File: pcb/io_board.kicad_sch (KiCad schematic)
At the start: 40 parts

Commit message: Further schematic capture
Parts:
- J?: value Barrel_Jack -> 9-15V DC
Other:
- note added: "ADAT Terminals"
- note added: "IDC Connector"
- note added: "Power Supply: 9-15V -SMPS-> 5V -LDO-> 3V3"
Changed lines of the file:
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@@
 		)
 	)
+	(text "IDC Connector"
+		(exclude_from_sim no)
+		(at 54.356 77.724 0)
+		(effects
+			(font
+				(size 2.54 2.54)
+				(thickness 0.3175)
+			)
+		)
+	)
+	(text "Power Supply: 9-15V -SMPS-> 5V -LDO-> 3V3"
+		(exclude_from_sim no)
+		(at 147.828 19.558 0)
+		(effects
+			(font
+				(size 2.54 2.54)
+				(thickness 0.3175)
+			)
+		)
+	)
+	(text "ADAT Terminals"
+		(exclude_from_sim no)
+		(at 186.69 80.518 0)
+		(effects
+			(font
+				(size 2.54 2.54)
+				(thickness 0.3175)
+			)
+		)
+	)
 	(junction
 		(at 186.69 35.56)
@@
 			)
 		)
-		(property "Value" "Barrel_Jack"
+		(property "Value" "9-15V DC"
 			(at 39.37 31.75 0)
 			(effects

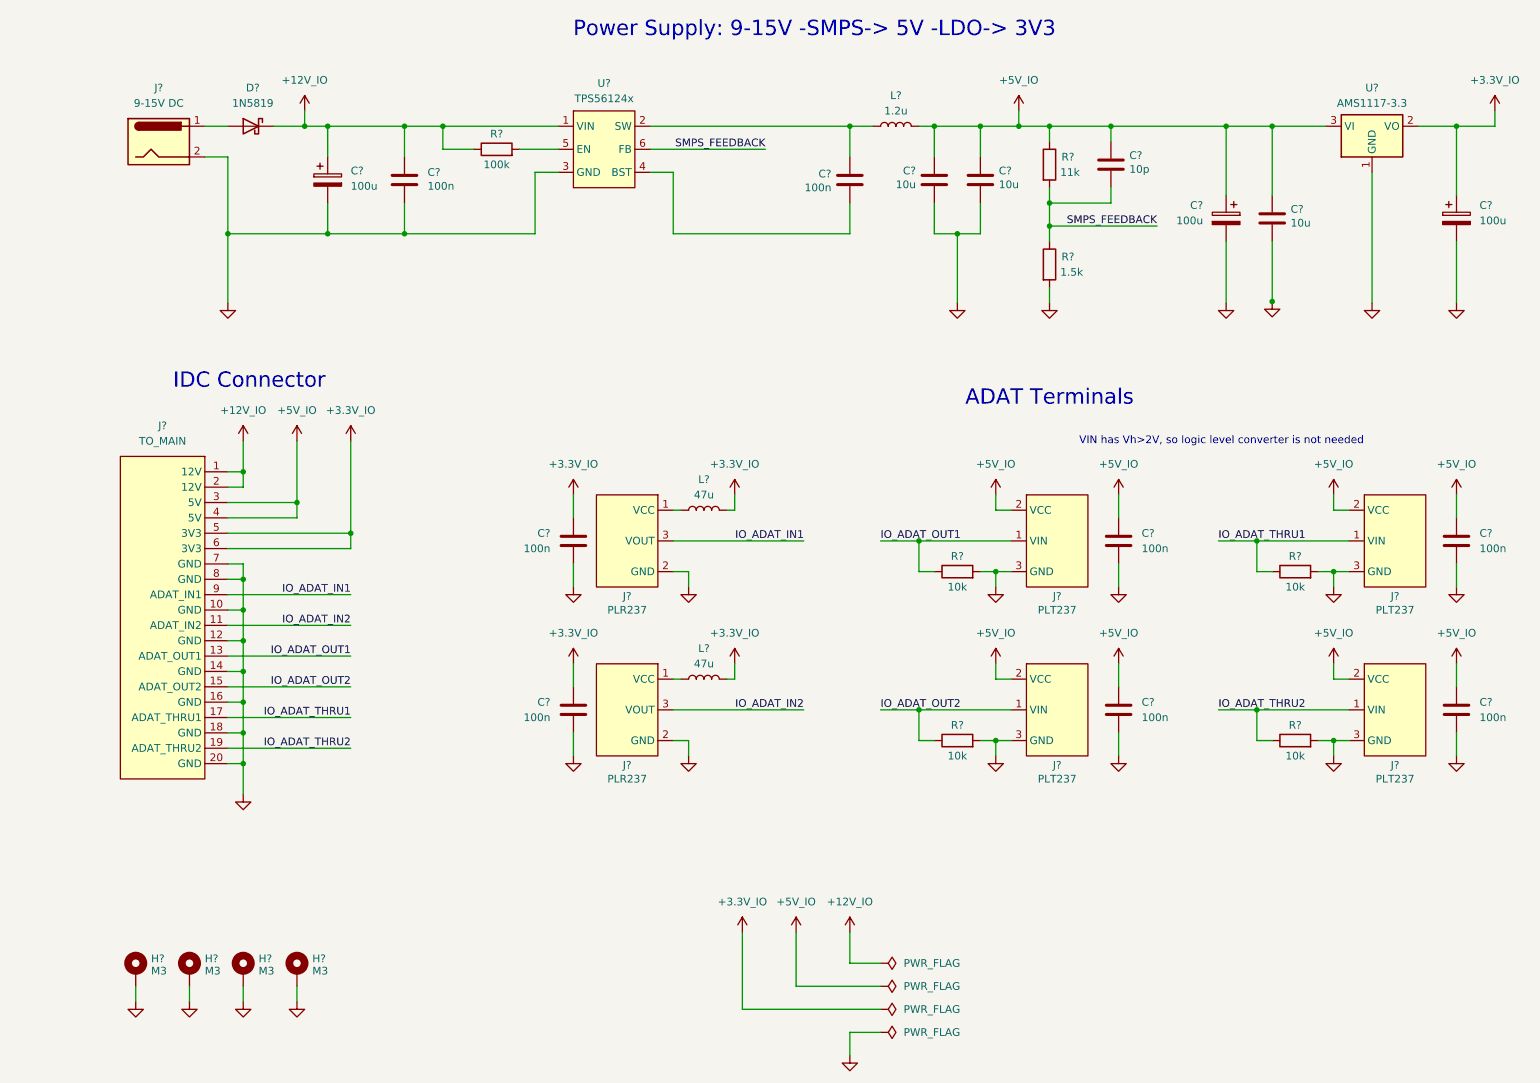
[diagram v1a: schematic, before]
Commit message: Assign most of the footprints to schematic components
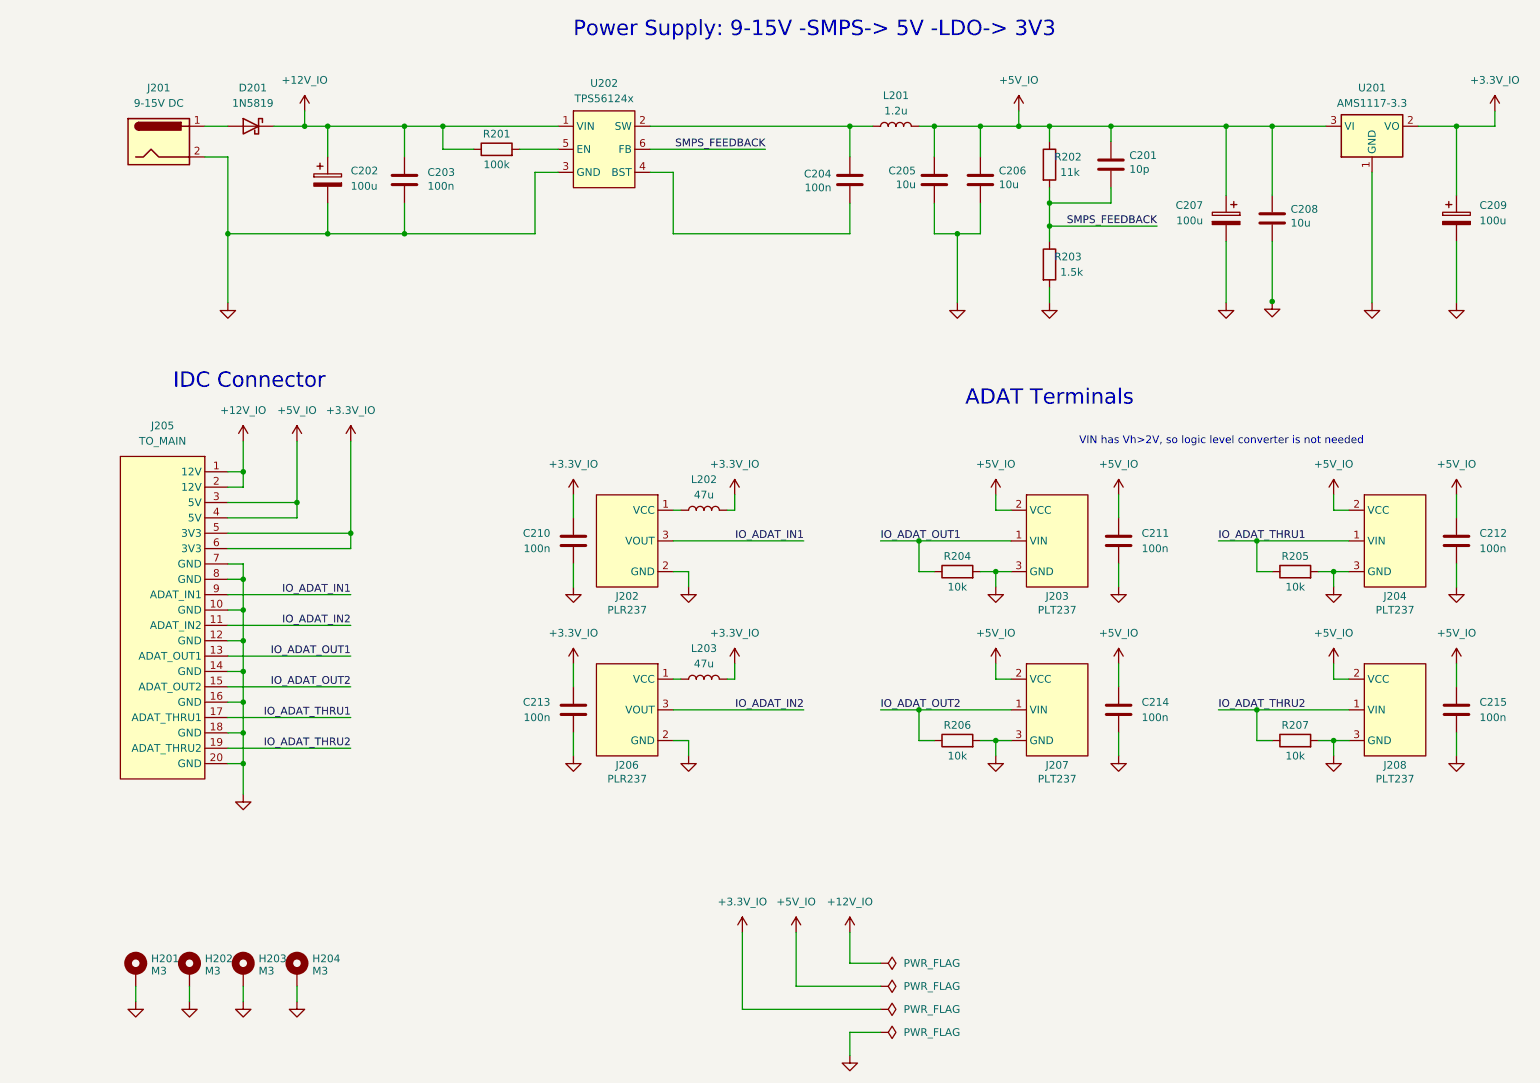
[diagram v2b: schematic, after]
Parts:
- C201, C203, C204, C205, C206, C208, C210, C211, C212, C213, C214, C215: renamed from C?; footprint (none) -> Capacitor_SMD:C_0805_2012Metric_Pad1.18x1.45mm_HandSolder
- C202, C207, C209: renamed from C?; footprint (none) -> Capacitor_SMD:C_Elec_6.3x5.4
- J205: renamed from J?; footprint (none) -> Connector_IDC:IDC-Header_2x10_P2.54mm_Vertical
- R201, R202, R203, R204, R205, R206, R207: renamed from R?; footprint (none) -> Resistor_SMD:R_0805_2012Metric_Pad1.20x1.40mm_HandSolder
- gave numbers to parts that had none: 17

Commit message: Finish assigning footprints to project
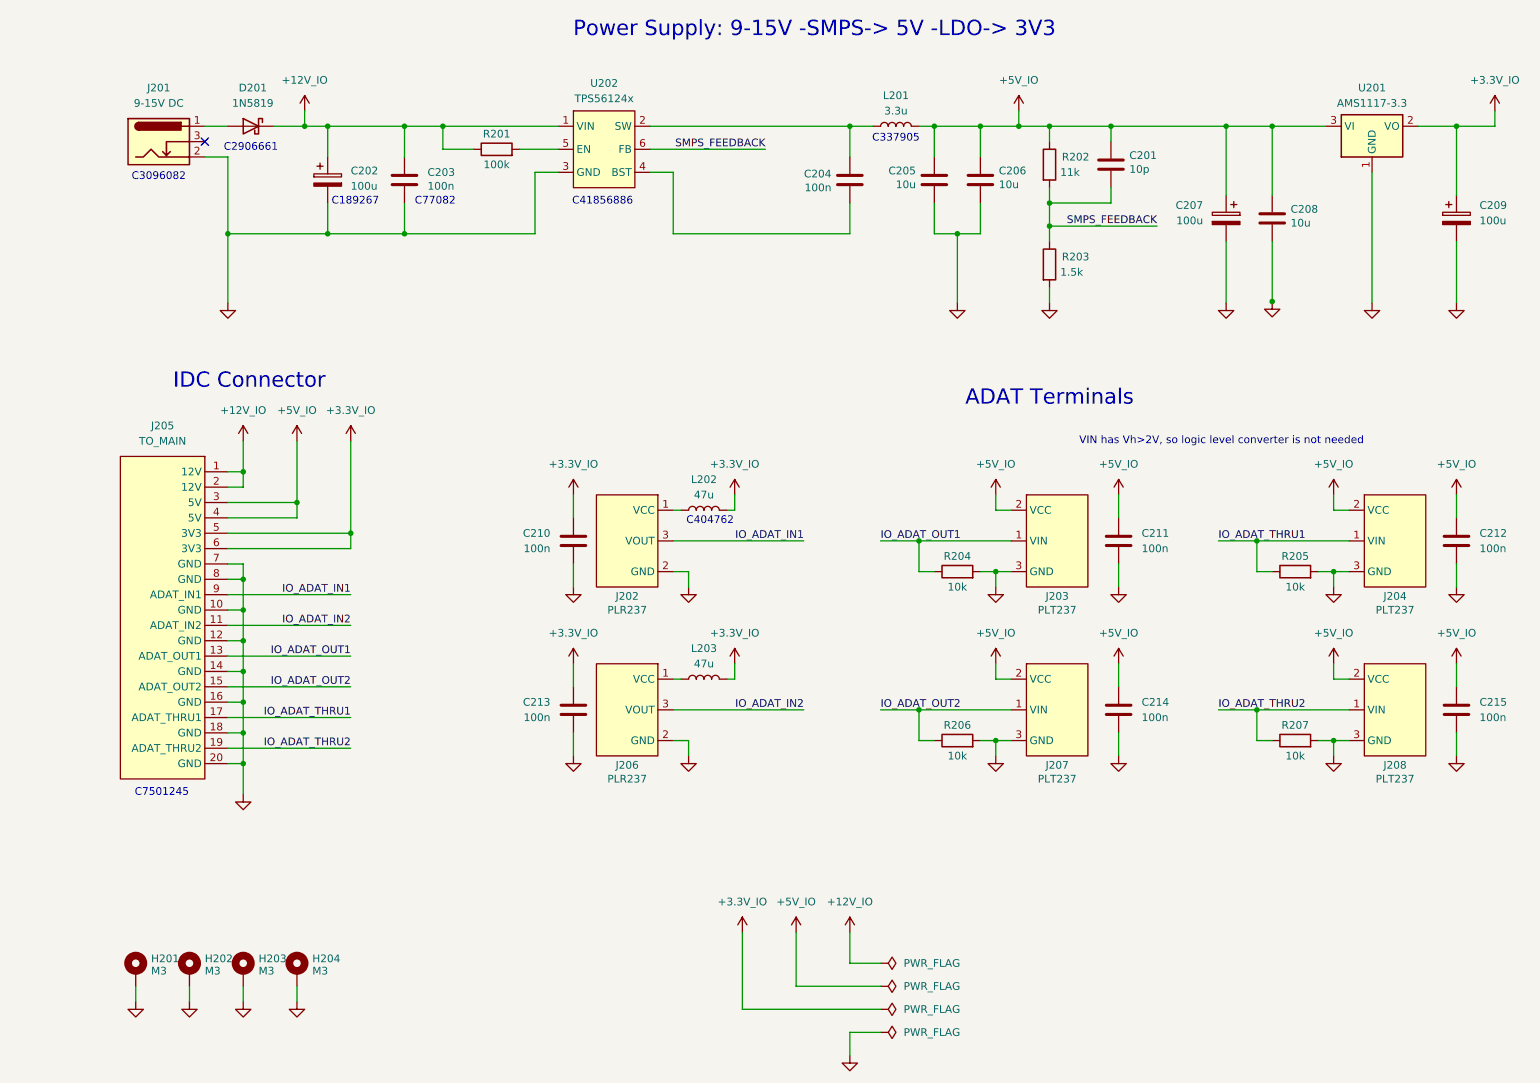
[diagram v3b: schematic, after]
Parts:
- removed J201: 9-15V DC, symbol Connector:Barrel_Jack
- added J201: 9-15V DC, adatv2:CUI PJ-002A, symbol Connector:Barrel_Jack_Switch
- L201: value 1.2u -> 3.3u; footprint (none) -> Inductor_SMD:L_1210_3225Metric_Pad1.42x2.65mm_HandSolder
- L202, L203: footprint (none) -> Inductor_SMD:L_0805_2012Metric_Pad1.15x1.40mm_HandSolder
- U202: footprint (none) -> Package_TO_SOT_SMD:SOT-563
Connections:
- net GND_IO: now also J201.2
- net at D201.2 (A): now also J201.1
- no-connect marks 0 -> 1
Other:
- note added: "C189267"
- note added: "C2906661"
- note added: "C3096082"
- note added: "C337905"
- note added: "C404762"
- note added: "C41856886"
- note added: "C7501245"
- note added: "C77082"
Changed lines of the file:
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@@
 		(comment 1 "Drawn by Łukasz Świszcz")
 	)
+	(text "C41856886"
+		(exclude_from_sim no)
+		(at 112.776 48.006 0)
+		(effects
+			(font
+				(size 1.27 1.27)
+			)
+		)
+	)
+	(text "C189267"
+		(exclude_from_sim no)
+		(at 71.882 48.006 0)
+		(effects
+			(font
+				(size 1.27 1.27)
+			)
+		)
+	)
+	(text "C404762"
+		(exclude_from_sim no)
+		(at 130.556 100.838 0)
+		(effects
+			(font
+				(size 1.27 1.27)
+			)
+		)
+	)
+	(text "C3096082"
+		(exclude_from_sim no)
+		(at 39.37 43.942 0)
+		(effects
+			(font
+				(size 1.27 1.27)
+			)
+		)
+	)
+	(text "C337905"
+		(exclude_from_sim no)
+		(at 161.29 37.592 0)
+		(effects
+			(font
+				(size 1.27 1.27)
+			)
+		)
+	)
+	(text "C2906661"
+		(exclude_from_sim no)
+		(at 54.61 39.116 0)
+		(effects
+			(font
+				(size 1.27 1.27)
+			)
+		)
+	)
+	(text "C7501245"
+		(exclude_from_sim no)
+		(at 39.878 145.796 0)
+		(effects
+			(font
+				(size 1.27 1.27)
+			)
+		)
+	)
 	(text "VIN has Vh>2V, so logic level converter is not needed"
 		(exclude_from_sim no)
@@
 		)
 	)
+	(text "C77082"
+		(exclude_from_sim no)
+		(at 85.09 48.006 0)
+		(effects
+			(font
+				(size 1.27 1.27)
+			)
+		)
+	)
 	(text "IDC Connector"
 		(exclude_from_sim no)
@@
 		(color 0 0 0 0)
 	)
+	(no_connect
+		(at 46.99 38.1)
+	)
 	(wire
 		(pts
@@
 	)
 	(symbol
+		(lib_id "Connector:Barrel_Jack_Switch")
+		(at 39.37 38.1 0)
+		(unit 1)
+		(exclude_from_sim no)
+		(in_bom yes)
+		(on_board yes)
+		(dnp no)
+		(fields_autoplaced yes)
+		(property "Reference" "J201"
+			(at 39.37 29.21 0)
+			(effects
+				(font
+					(size 1.27 1.27)
+				)
+			)
+		)
+		(property "Value" "9-15V DC"
+			(at 39.37 31.75 0)
+			(effects
+				(font
+					(size 1.27 1.27)
+				)
+			)
+		)
+		(property "Footprint" "adatv2:CUI PJ-002A"
+			(at 40.64 39.116 0)
+			(effects
+				(font
+					(size 1.27 1.27)
+				)
+				(hide yes)
+			)
+		)
+		(property "Datasheet" "~"
+			(at 40.64 39.116 0)
+			(effects
+				(font
+					(size 1.27 1.27)
+				)
+				(hide yes)
+			)
+		)
+		(property "Description" "DC Barrel Jack with an internal switch"
+			(at 39.37 38.1 0)
+			(effects
+				(font
+					(size 1.27 1.27)
+				)
+				(hide yes)
+			)
+		)
+		(pin "3"
+		)
+		(pin "1"
+		)
+		(pin "2"
+		)
+		(instances
+			(project ""
+				(path "/81929cdc-f9fd-4c47-8b7e-bc8597104756/2798f55d-c401-4d3b-b8be-ffe1fd6e245a"
+					(reference "J201")
+					(unit 1)
+				)
+			)
+		)
+	)
+	(symbol
 		(lib_id "power:GND")
 		(at 107.95 139.7 0)
@@
 			)
 		)
-		(property "Footprint" ""
+		(property "Footprint" "Inductor_SMD:L_0805_2012Metric_Pad1.15x1.40mm_HandSolder"
 			(at 129.54 127 0)
 			(effects
@@
 		(dnp no)
 		(property "Reference" "R202"
-			(at 189.738 40.64 0)
+			(at 191.008 40.64 0)
 			(effects
 				(font
@@
 		(dnp no)
 		(property "Reference" "R203"
-			(at 189.738 57.15 0)
+			(at 191.008 57.15 0)
 			(effects
 				(font
@@
 			)
 		)
-		(property "Footprint" ""
+		(property "Footprint" "Inductor_SMD:L_0805_2012Metric_Pad1.15x1.40mm_HandSolder"
 			(at 129.54 99.06 0)
 			(effects
@@
 	)
 	(symbol
-		(lib_id "Connector:Barrel_Jack")
-		(at 39.37 38.1 0)
-		(unit 1)
-		(exclude_from_sim no)
-		(in_bom yes)
-		(on_board yes)
-		(dnp no)
-		(fields_autoplaced yes)
-		(property "Reference" "J201"
-			(at 39.37 29.21 0)
-			(effects
-				(font
-					(size 1.27 1.27)
-				)
-			)
-		)
-		(property "Value" "9-15V DC"
-			(at 39.37 31.75 0)
-			(effects
-				(font
-					(size 1.27 1.27)
-				)
-			)
-		)
-		(property "Footprint" ""
-			(at 40.64 39.116 0)
-			(effects
-				(font
-					(size 1.27 1.27)
-				)
-				(hide yes)
-			)
-		)
-		(property "Datasheet" "~"
-			(at 40.64 39.116 0)
-			(effects
-				(font
-					(size 1.27 1.27)
-				)
-				(hide yes)
-			)
-		)
-		(property "Description" "DC Barrel Jack"
-			(at 39.37 38.1 0)
-			(effects
-				(font
-					(size 1.27 1.27)
-				)
-				(hide yes)
-			)
-		)
-		(pin "1"
-		)
-		(pin "2"
-		)
-		(instances
-			(project "adatv2"
-				(path "/81929cdc-f9fd-4c47-8b7e-bc8597104756/2798f55d-c401-4d3b-b8be-ffe1fd6e245a"
-					(reference "J201")
-					(unit 1)
-				)
-			)
-		)
-	)
-	(symbol
 		(lib_id "power:PWR_FLAG")
 		(at 158.75 181.61 270)
@@
 			)
 		)
-		(property "Value" "1.2u"
+		(property "Value" "3.3u"
 			(at 161.29 33.02 90)
 			(effects
@@
 			)
 		)
-		(property "Footprint" ""
+		(property "Footprint" "Inductor_SMD:L_1210_3225Metric_Pad1.42x2.65mm_HandSolder"
 			(at 161.29 35.56 0)
 			(effects
@@
 			)
 		)
-		(property "Footprint" ""
+		(property "Footprint" "Package_TO_SOT_SMD:SOT-563"
 			(at 113.03 39.37 0)
 			(effects

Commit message: Finish drawing IO/Supply board
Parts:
- added TP201, TP202, TP203: ${NET_NAME(1)}, TestPoint:TestPoint_Pad_D2.5mm, symbol Connector:TestPoint
- C205, C206, C208: footprint Capacitor_SMD:C_0805_2012Metric_Pad1.18x1.45mm_HandSolder -> Capacitor_SMD:C_1206_3216Metric_Pad1.33x1.80mm_HandSolder
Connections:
- net GND is gone; now on net GND_IO: H201.1, H202.1, H203.1, H204.1
- net +12V_IO: now also TP201.1
- net +3.3V_IO: now also L202.1, L203.1, TP203.1; no longer C210.1, C213.1, L202.2, L203.2
- net +5V_IO: now also TP202.1
- net POWER_IN: now reaches D201.2 (A), J201.1
- net at J206.1 (VCC): now also C213.1, L203.2; no longer L203.1
- net at J202.1 (VCC): now also C210.1, L202.2; no longer L202.1
- net SMPS_POWER_OUT: now reaches C204.1, L201.1, U202.2 (SW)
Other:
- moved on the sheet: J201, L202, L203

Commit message: Add buffers for ADAT transfer
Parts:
- added C216: 100n, Capacitor_SMD:C_0805_2012Metric_Pad1.18x1.45mm_HandSolder, symbol Device:C
- added U203: 74LVC2G17, Package_TO_SOT_SMD:SOT-23-6_Handsoldering, symbol 74xGxx:74LVC2G17
- R204, R205, R206, R207: value 10k -> 1k
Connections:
- net +3.3V_IO: now also C216.1, U203.5 (VCC)
- net GND_IO: now also C216.2, U203.2 (GND)
- net IO_ADAT_IN1: now also U203.6; no longer J202.3 (VOUT)
- net IO_ADAT_IN2: now also U203.4; no longer J206.3 (VOUT)
- new net: J202.3 (VOUT), U203.1
- new net: J206.3 (VOUT), U203.3
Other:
- moved on the sheet: C210, C213, H201, H202, H203, H204, J202, J205, J206, L202, L203

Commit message: Assign FPGA pins, change MCU to STM32F429VET6
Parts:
- R204, R205, R206, R207: value 1k -> 150
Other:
- note added: "Output Buffers"
- moved on the sheet: C216, H201, H202, H203, H204, TP201, TP202, TP203, U203C
